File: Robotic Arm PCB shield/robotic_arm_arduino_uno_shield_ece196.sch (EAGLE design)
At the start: 34 parts, among them J1 (ID,OD)=(2.1,5.5)MM

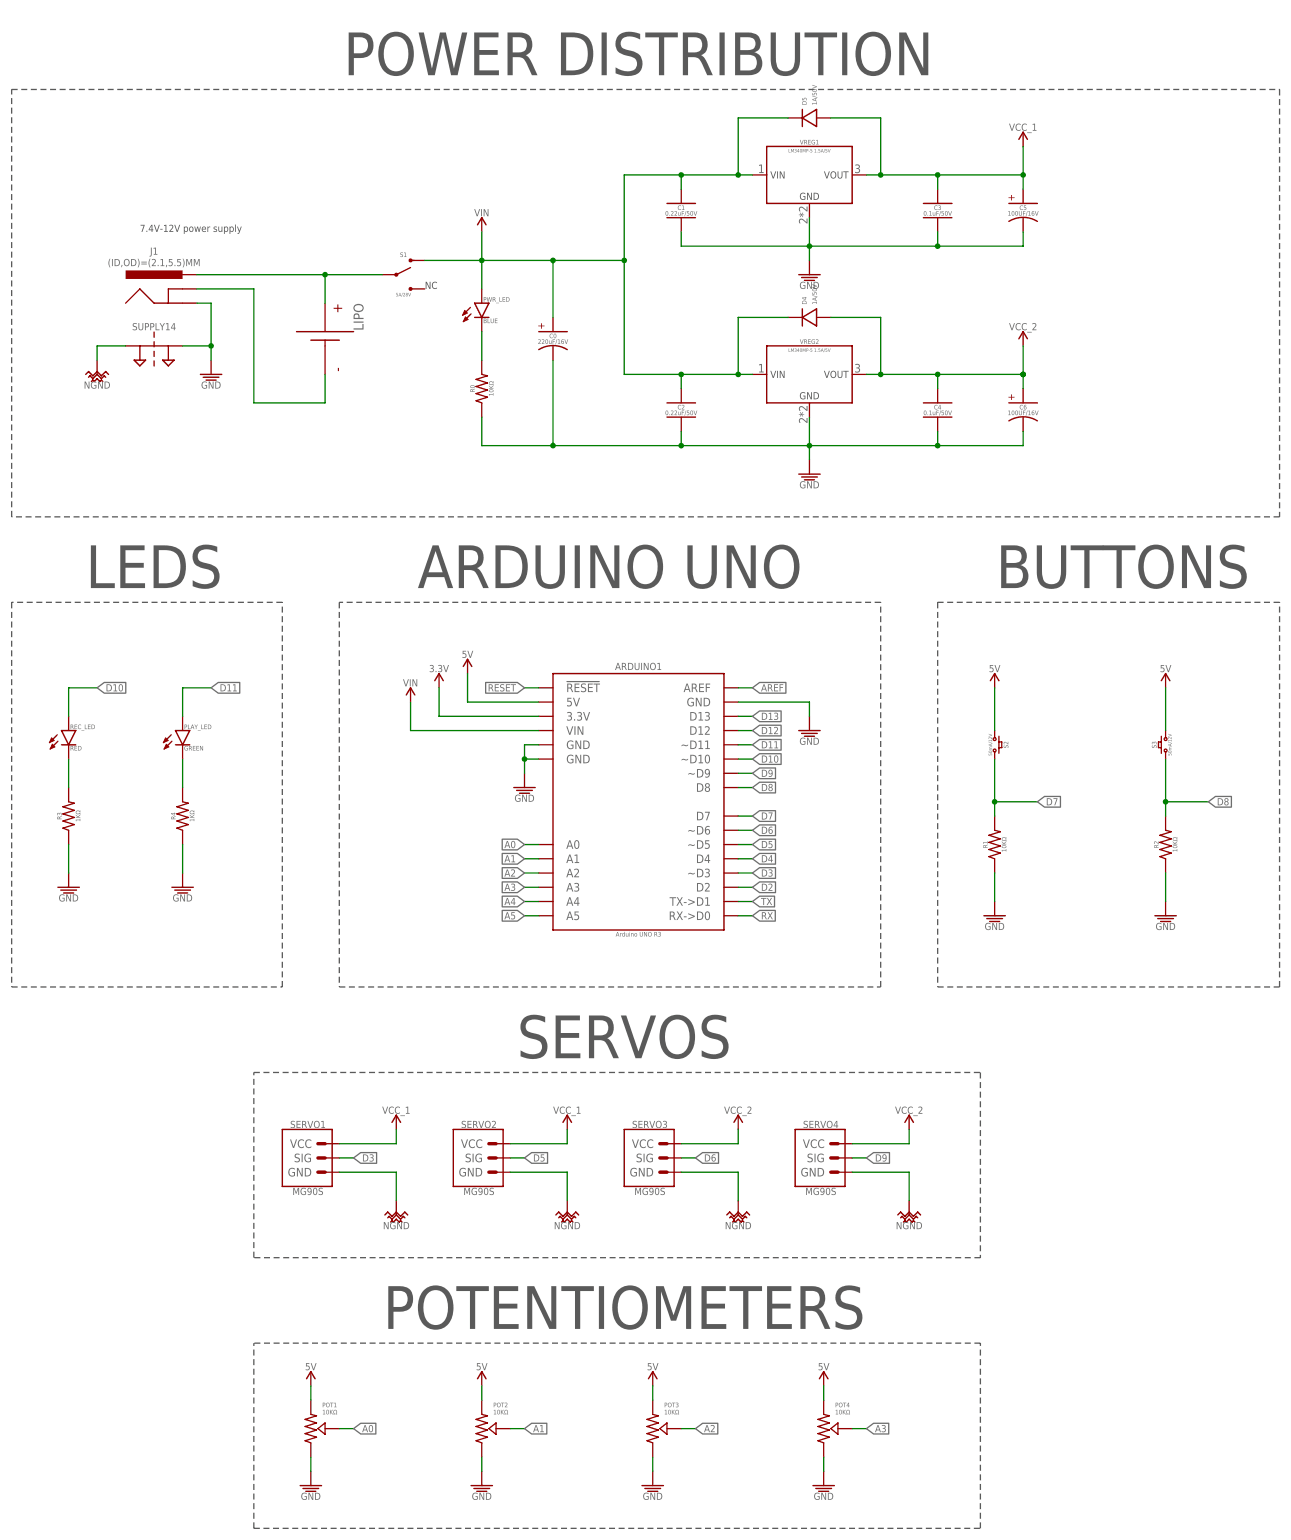
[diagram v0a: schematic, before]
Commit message: Rev 5:  Add 1000uF capacitors for potential performance boost by reducing any ripple.  Add tons of vias by voltage regulators to help with heat dissipation.  Update all components to newest libraries.
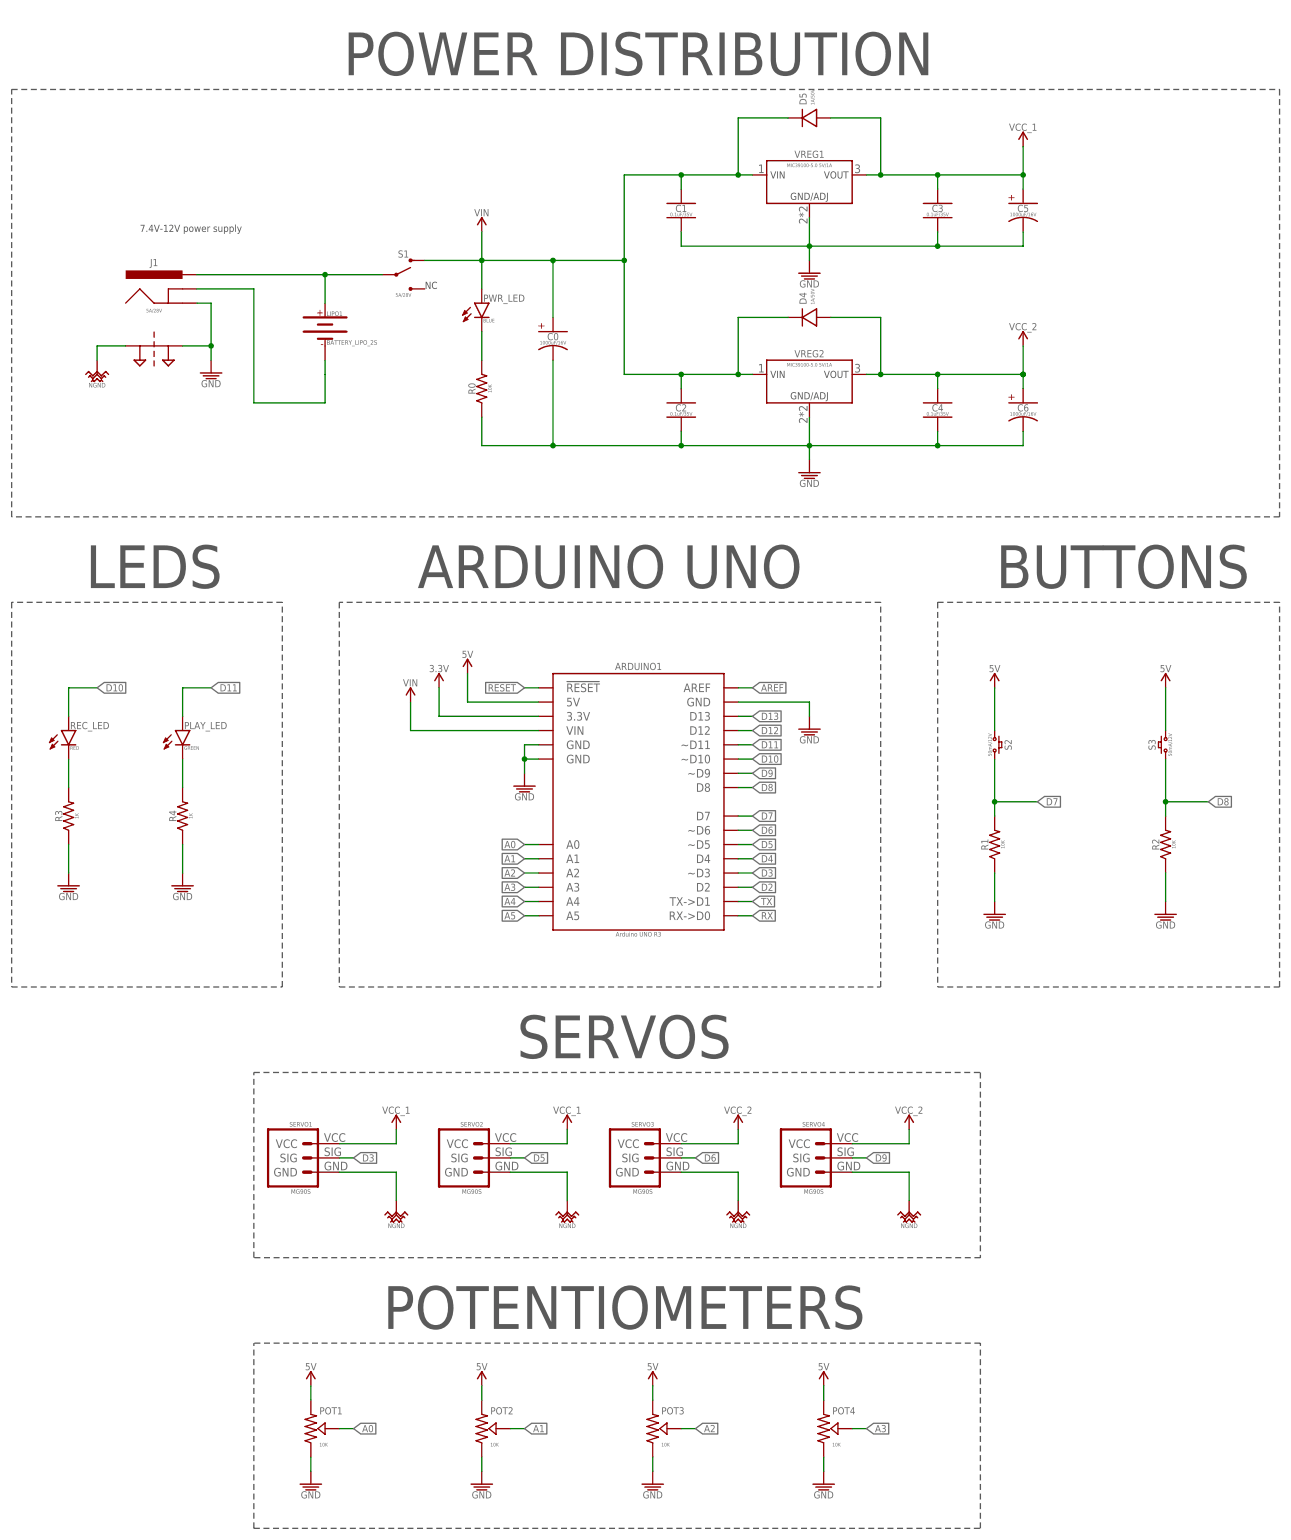
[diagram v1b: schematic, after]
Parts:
- removed LIPO: 7.4V, PiB_batteries:BATTERY_LIPO_BATTERY
- added LIPO1: BATTERY_LIPO_2S, PiB_batteries:BATTERY_LIPO_2S
- C0: value 220uF/16V -> 1000uF/16V; device PiB_capacitors:220UF-POLARIZED_SMD_16V-20% -> PiB_capacitors:1000UF-POLARIZED_PTH_16V-20%
- C1, C2: value 0.22uF/50V -> 0.1uF/35V; device PiB_capacitors:0.22UF_SMD-805_50V-10% -> PiB_capacitors:0.1UF_SMD-0805_35V-10%
- C3, C4: value 0.1uF/50V -> 0.1uF/35V; device PiB_capacitors:0.1UF_SMD-805_50V-10% -> PiB_capacitors:0.1UF_SMD-0805_35V-10%
- C5, C6: value 100UF/16V -> 1000uF/16V; device PiB_capacitors:100UF-POLARIZED_SMD_16V-20% -> PiB_capacitors:1000UF-POLARIZED_PTH_16V-20%
- J1: value (ID,OD)=(2.1,5.5)MM -> 5A/28V; device PiB_connectors:POWER_JACK-BARREL_ID2.1MM-OD5.5MMPTH -> PiB_connectors:POWER_JACK-BARREL_ID2.1MM-OD5.5MM_PTH_ID2.1MM-OD5.5MM
- POT1, POT2, POT3, POT4: value 10KΩ -> 10K; device PiB_resistors:POTENTIOMETER_NO-MARKINGS_VERT-FEMALE -> PiB_resistors:POTENTIOMETER_CONNECTOR_PTH_VERT_FEMALE_2.54MM
- R0, R1, R2: value 10KΩ -> 10K
- R3, R4: value 1KΩ -> 1K
- S1: device PiB_switches:SWITCH_SPDT_VERT_PTH_5A-28V_13L-7W -> PiB_switches:SWITCH_SPDT_VERT_PTH_5A-28V_13L-7W_
- S2, S3: device PiB_switches:SWITCH_MOMENTARYSPST-PTH-L12-W12-H7.2 -> PiB_switches:SWITCH_MOMENTARY_SPST_PTH_L12-W12-H7.2
- SERVO1, SERVO2, SERVO3, SERVO4: device PiB:SERVOMG90S -> PiB_motors:SERVO_MG90S_PTH_VERT_FEMALE_2.54MM
- SUPPLY14: value 2PT_GND_TIE -> NET_BRIDGE; device PiB_power_symbols:2PT_GND_TIE -> PiB_power_symbols:NET_BRIDGE
- VREG1, VREG2: value LM340MP-5 1.5A/5V -> MIC39100-5.0 5V/1A; device PiB_ic_power:VREG_LINEAR_FIXED_LM340MP-5_1.5A-5V -> PiB_ic_power:MIC39100-XX_MIC39100-5.0_1A
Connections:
- net +: now also LIPO1.P$1, S1.P; no longer LIPO.P, S1.2
- net -: now also J1.GND_BATTERY, LIPO1.P$2; no longer J1.GND@1, LIPO.N
- net GND: now also J1.GND_JACK; no longer J1.GND@2
- net VIN: now also S1.S1; no longer S1.1
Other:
- moved on the sheet: VREG1, VREG2
